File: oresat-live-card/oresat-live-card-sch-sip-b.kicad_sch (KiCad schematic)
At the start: 24 parts, among them U23 RCLAMP0504FB, U7 OSD3358-512M-BSM, Y1 24MHz, Y2 32.768KHZ

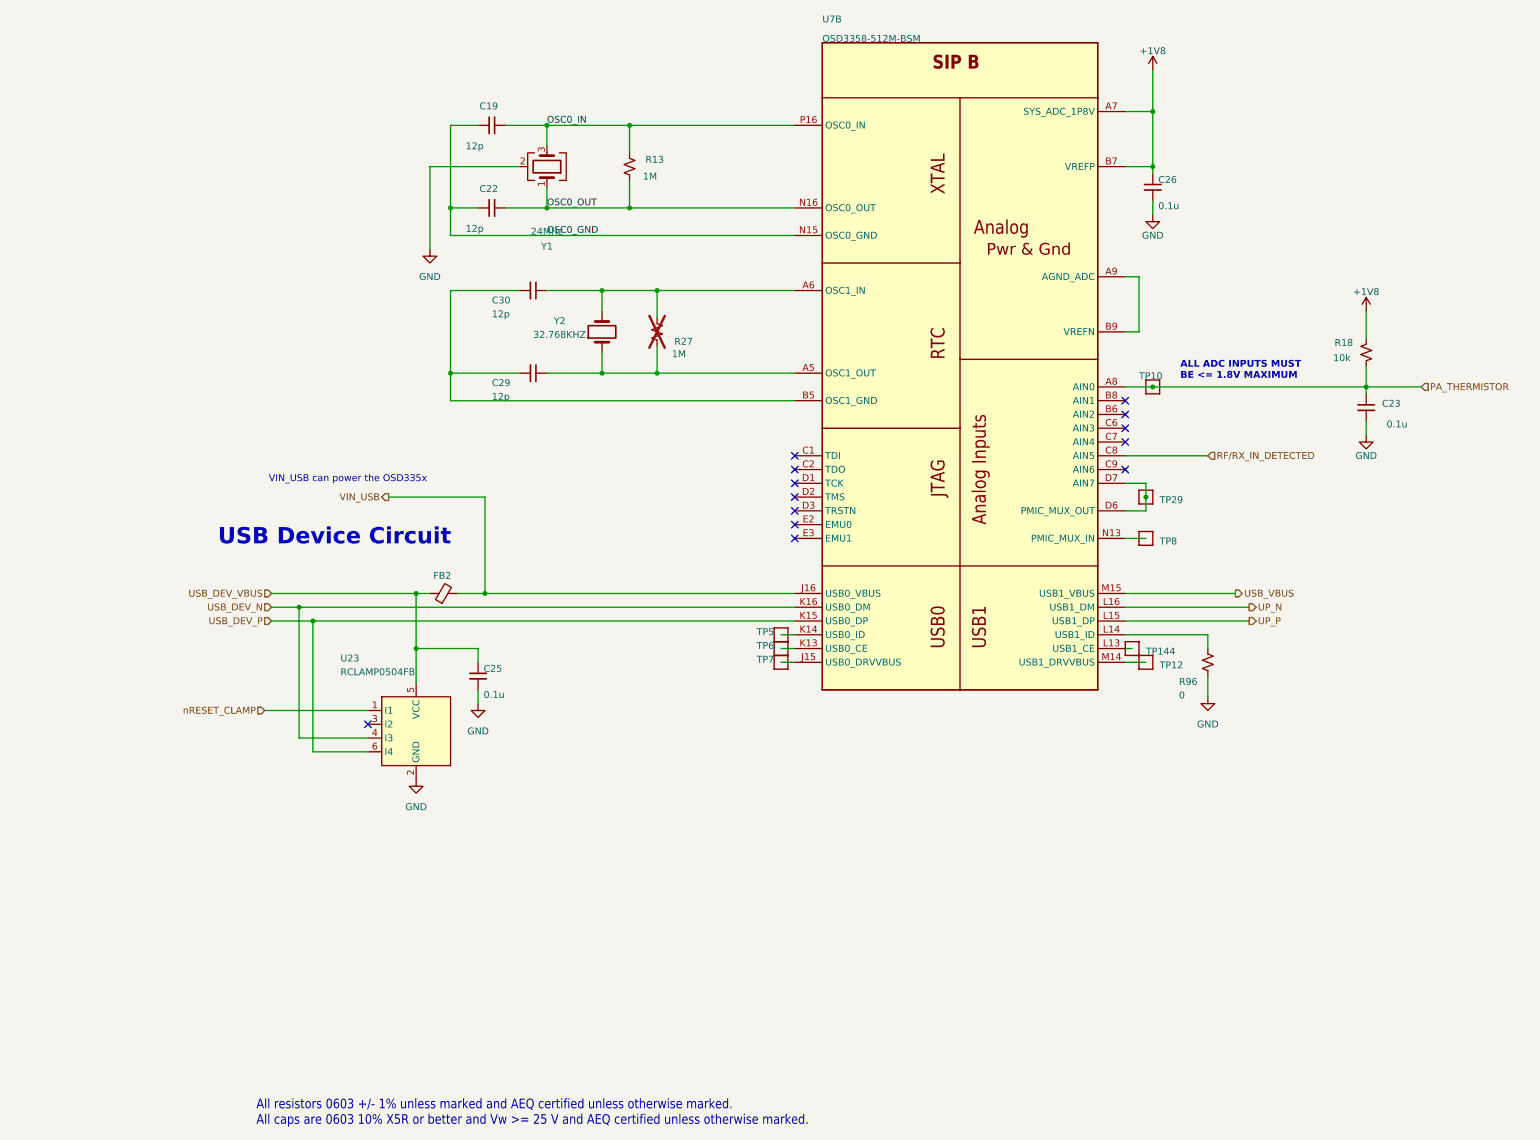
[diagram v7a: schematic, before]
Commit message: More schematic cleanup, sync between sch/brd, and some board cleanup. No more DRCs.
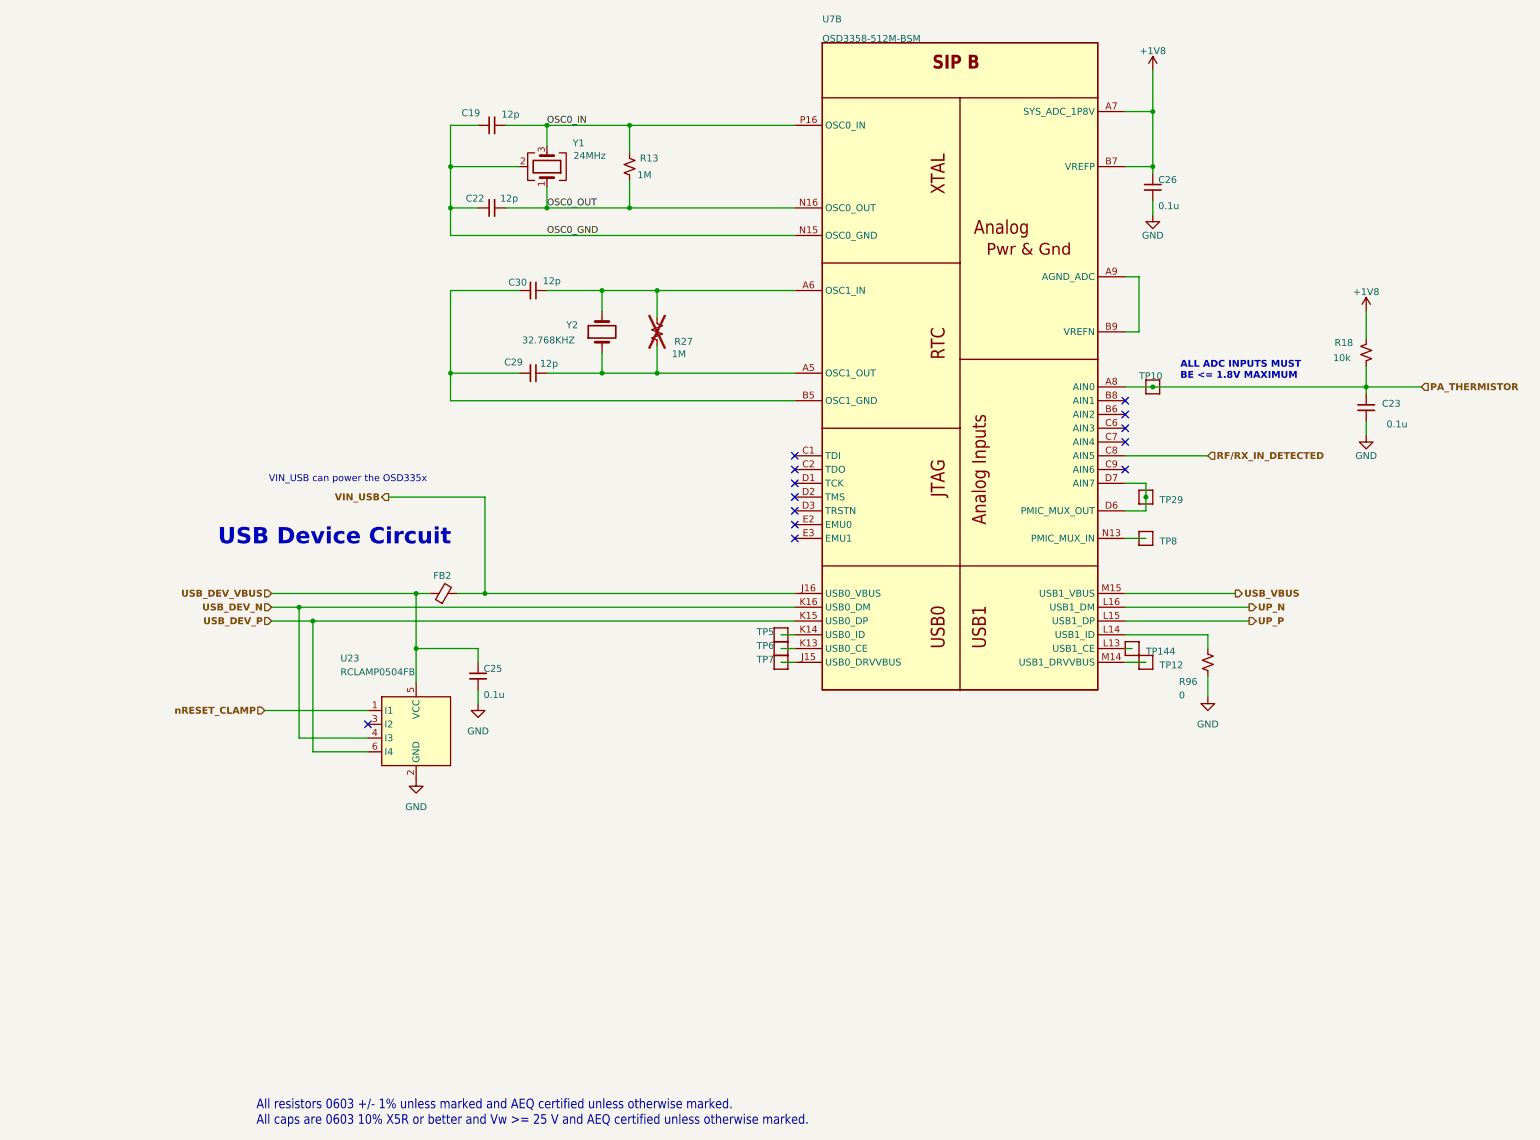
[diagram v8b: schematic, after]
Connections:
- net GND: no longer Y1.2 (G), Y1.4 (G)
- net OSC0_GND: now also Y1.2 (G), Y1.4 (G)
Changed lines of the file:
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@@
 	)
 	(junction
+		(at 148.59 88.9)
+		(diameter 0)
+		(color 0 0 0 0)
+	)
+	(junction
 		(at 142.24 167.64)
 		(diameter 0)
@@
 	(wire
 		(pts
+			(xy 148.59 88.9) (xy 161.29 88.9)
+		)
+		(stroke
+			(width 0)
+			(type default)
+		)
+	)
+	(wire
+		(pts
 			(xy 186.69 111.76) (xy 186.69 116.84)
 		)
@@
 	(wire
 		(pts
+			(xy 148.59 88.9) (xy 148.59 81.28)
+		)
+		(stroke
+			(width 0)
+			(type default)
+		)
+	)
+	(wire
+		(pts
 			(xy 148.59 127) (xy 148.59 132.08)
 		)
@@
 	(wire
 		(pts
-			(xy 148.59 96.52) (xy 148.59 81.28)
+			(xy 148.59 96.52) (xy 148.59 88.9)
 		)
 		(stroke
@@
 	(wire
 		(pts
-			(xy 144.78 88.9) (xy 161.29 88.9)
-		)
-		(stroke
-			(width 0)
-			(type default)
-		)
-	)
-	(wire
-		(pts
 			(xy 166.37 81.28) (xy 181.61 81.28)
 		)
@@
 	(wire
 		(pts
-			(xy 144.78 88.9) (xy 144.78 104.14)
-		)
-		(stroke
-			(width 0)
-			(type default)
-		)
-	)
-	(wire
-		(pts
 			(xy 209.55 177.8) (xy 212.09 177.8)
 		)
@@
 			(font
 				(size 1.27 1.27)
+				(thickness 0.254)
+				(bold yes)
 			)
 			(justify left)
@@
 			(font
 				(size 1.27 1.27)
+				(thickness 0.254)
+				(bold yes)
 			)
 			(justify left)
@@
 			(font
 				(size 1.27 1.27)
+				(thickness 0.254)
+				(bold yes)
 			)
 			(justify left)
@@
 			(font
 				(size 1.27 1.27)
+				(thickness 0.254)
+				(bold yes)
 			)
 			(justify right)
@@
 			(font
 				(size 1.27 1.27)
+				(thickness 0.254)
+				(bold yes)
 			)
 			(justify left)
@@
 			(font
 				(size 1.27 1.27)
+				(thickness 0.254)
+				(bold yes)
 			)
 			(justify right)
@@
 			(font
 				(size 1.27 1.27)
+				(thickness 0.254)
+				(bold yes)
 			)
 			(justify left)
@@
 			(font
 				(size 1.27 1.27)
+				(thickness 0.254)
+				(bold yes)
 			)
 			(justify right)
@@
 			(font
 				(size 1.27 1.27)
+				(thickness 0.254)
+				(bold yes)
 			)
 			(justify right)
@@
 			(font
 				(size 1.27 1.27)
+				(thickness 0.254)
+				(bold yes)
 			)
 			(justify right)
@@
 		(dnp no)
 		(property "Reference" "Y1"
-			(at 166.37 102.87 90)
+			(at 172.212 83.82 90)
 			(show_name no)
 			(do_not_autoplace no)
@@
 		)
 		(property "Value" "24MHz"
-			(at 166.37 101.6 90)
+			(at 174.244 87.63 90)
 			(show_name no)
 			(do_not_autoplace no)
@@
 	)
 	(symbol
-		(lib_id "power:GND")
-		(at 144.78 104.14 0)
-		(unit 1)
-		(body_style 1)
-		(exclude_from_sim no)
-		(in_bom yes)
-		(on_board yes)
-		(in_pos_files yes)
-		(dnp no)
-		(fields_autoplaced yes)
-		(property "Reference" "#PWR52"
-			(at 144.78 110.49 0)
-			(hide yes)
-			(show_name no)
-			(do_not_autoplace no)
-			(effects
-				(font
-					(size 1.27 1.27)
-				)
-			)
-		)
-		(property "Value" "GND"
-			(at 144.78 109.22 0)
-			(show_name no)
-			(do_not_autoplace no)
-			(effects
-				(font
-					(size 1.27 1.27)
-				)
-			)
-		)
-		(property "Footprint" ""
-			(at 144.78 104.14 0)
-			(hide yes)
-			(show_name no)
-			(do_not_autoplace no)
-			(effects
-				(font
-					(size 1.27 1.27)
-				)
-			)
-		)
-		(property "Datasheet" ""
-			(at 144.78 104.14 0)
-			(hide yes)
-			(show_name no)
-			(do_not_autoplace no)
-			(effects
-				(font
-					(size 1.27 1.27)
-				)
-			)
-		)
-		(property "Description" "Power symbol creates a global label with name \"GND\" , ground"
-			(at 144.78 104.14 0)
-			(hide yes)
-			(show_name no)
-			(do_not_autoplace no)
-			(effects
-				(font
-					(size 1.27 1.27)
-				)
-			)
-		)
-		(pin "1"
-		)
-		(instances
-			(project "oresat-live-card"
-				(path "/748bdd2d-da0a-4240-ba60-0bf881d2ec56/49f5f571-d1f9-4350-855b-6ca6690b0a90"
-					(reference "#PWR52")
-					(unit 1)
-				)
-			)
-		)
-	)
-	(symbol
 		(lib_id "Device:R_Small_US")
 		(at 181.61 88.9 180)
@@
 		(dnp no)
 		(property "Reference" "R13"
-			(at 187.96 86.868 0)
+			(at 186.944 86.614 0)
 			(show_name no)
 			(do_not_autoplace no)
@@
 		)
 		(property "Value" "1M"
-			(at 186.69 91.44 0)
+			(at 185.674 91.186 0)
 			(show_name no)
 			(do_not_autoplace no)
@@
 		(dnp no)
 		(property "Reference" "C30"
-			(at 156.21 114.3 90)
+			(at 159.258 110.998 90)
 			(show_name no)
 			(do_not_autoplace no)
@@
 		)
 		(property "Value" "12p"
-			(at 156.21 116.84 90)
+			(at 165.608 110.744 90)
 			(show_name no)
 			(do_not_autoplace no)
@@
 		(dnp no)
 		(property "Reference" "C29"
-			(at 156.21 129.54 90)
+			(at 158.496 125.73 90)
 			(show_name no)
 			(do_not_autoplace no)
@@
 		)
 		(property "Value" "12p"
-			(at 156.21 132.08 90)
+			(at 165.1 125.984 90)
 			(show_name no)
 			(do_not_autoplace no)
@@
 		(dnp no)
 		(property "Reference" "Y2"
-			(at 167.64 118.11 90)
+			(at 169.926 118.872 90)
 			(show_name no)
 			(do_not_autoplace no)
@@
 		)
 		(property "Value" "32.768KHZ"
-			(at 163.83 120.65 90)
+			(at 161.798 121.666 90)
 			(show_name no)
 			(do_not_autoplace no)
@@
 		(dnp no)
 		(property "Reference" "C19"
-			(at 153.924 78.486 90)
+			(at 150.622 79.756 90)
 			(show_name no)
 			(do_not_autoplace no)
@@
 		)
 		(property "Value" "12p"
-			(at 151.384 85.852 90)
+			(at 157.988 80.01 90)
 			(show_name no)
 			(do_not_autoplace no)
@@
 		(dnp no)
 		(property "Reference" "C22"
-			(at 153.924 93.726 90)
+			(at 151.384 95.504 90)
 			(show_name no)
 			(do_not_autoplace no)
@@
 		)
 		(property "Value" "12p"
-			(at 151.384 101.092 90)
+			(at 157.734 95.504 90)
 			(show_name no)
 			(do_not_autoplace no)
